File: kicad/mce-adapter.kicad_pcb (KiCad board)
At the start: 2 copper layers, 65.2 x 31.6 mm, 18 parts, among them J123 Conn_02x03_Odd_Even, J4 Conn_01x03_Male, U1 GAL16V8

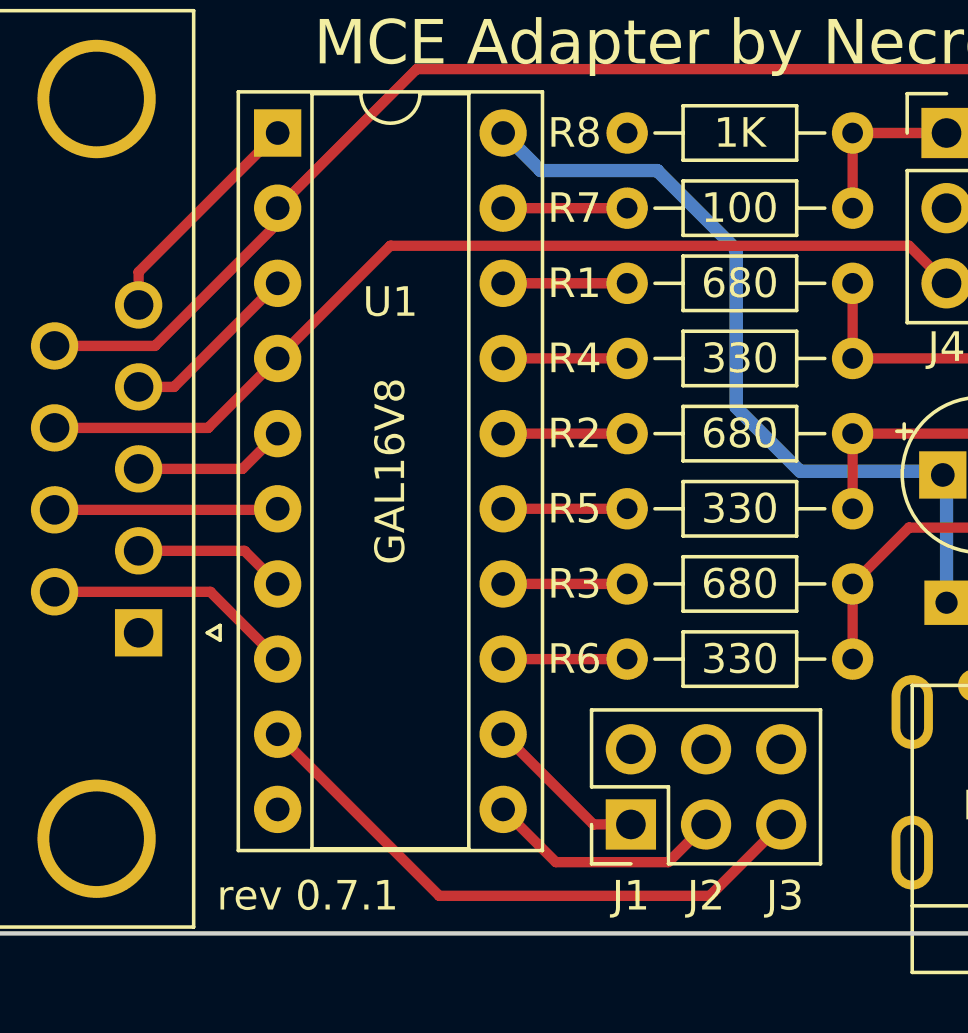
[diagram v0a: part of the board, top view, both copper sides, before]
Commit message: Readjusted resistor values, updated to version 0.7.2
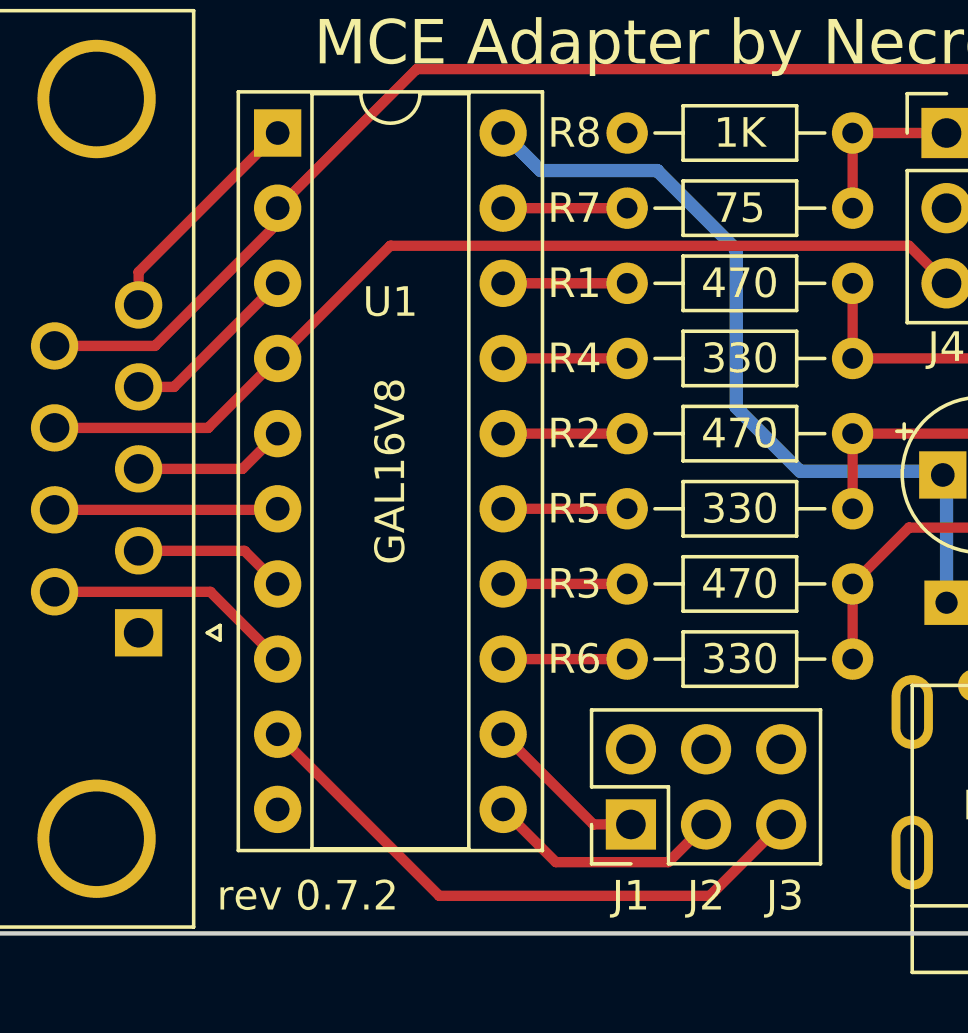
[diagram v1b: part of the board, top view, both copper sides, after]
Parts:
- R1, R2, R3: value 680 -> 470
- R7: value 100 -> 75
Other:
- board text added: "rev 0.7.2"
- board text removed: "rev 0.7.1"

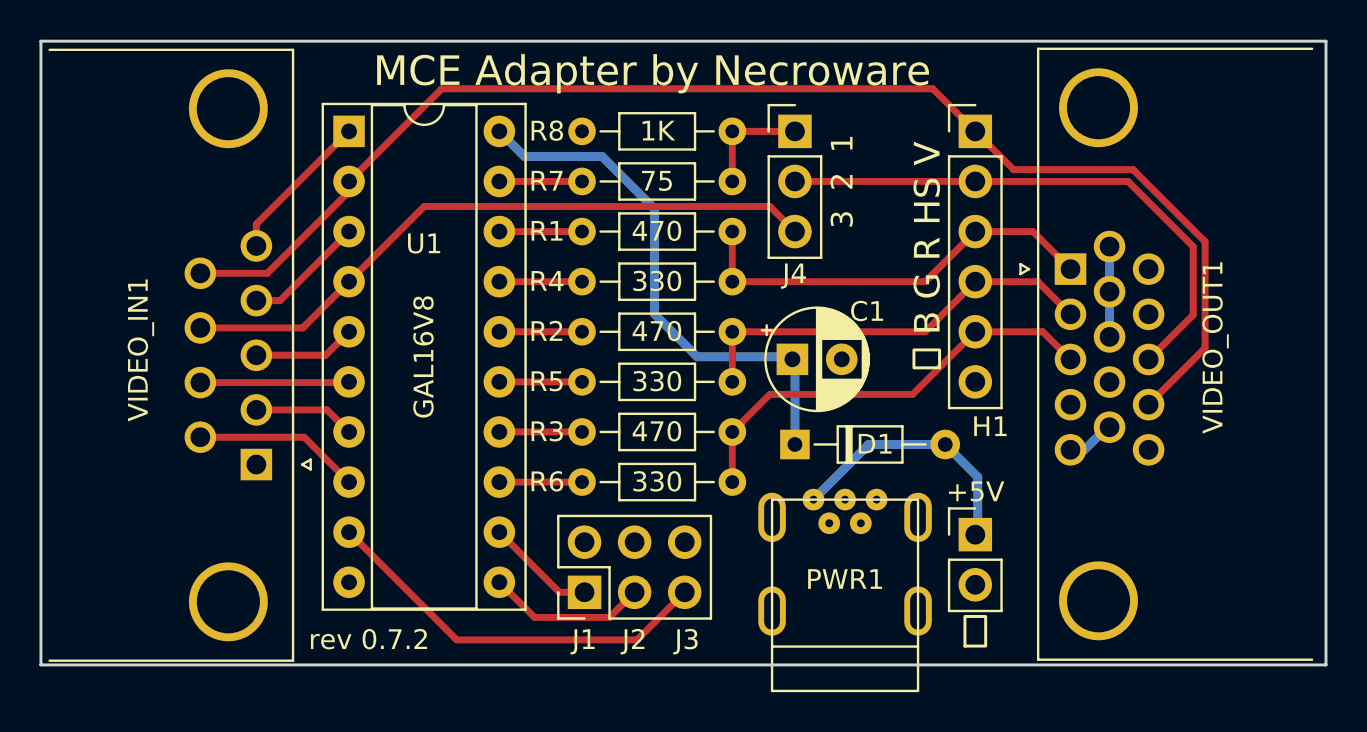
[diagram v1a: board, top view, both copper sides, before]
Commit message: Re-added DIP switch, rev. 0.8.0
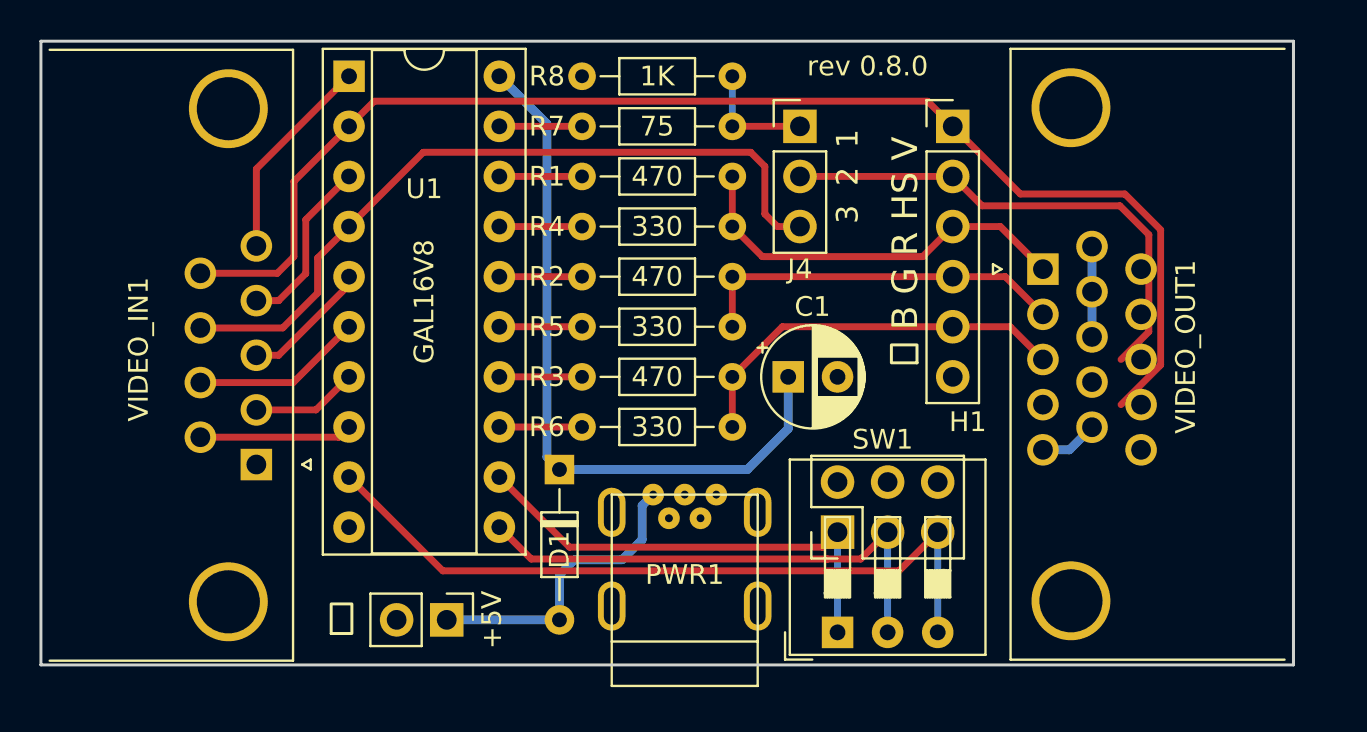
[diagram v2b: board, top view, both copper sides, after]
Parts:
- added REF**: OSHW-Symbol_6.7x6mm_SilkScreen, Symbol:OSHW-Symbol_6.7x6mm_SilkScreen, F.Cu at (169.8, 113.8)
- added SW1: SW_DIP_x03, Button_Switch_THT:SW_DIP_SPSTx03_Slide_9.78x9.8mm_W7.62mm_P2.54mm, F.Cu at (151.1, 116.7)
- moved PWR2 27.1 mm to (131.3, 116.1), turned to 270 degrees
- moved J123 13.2 mm to (151.1, 111.6)
- moved D1 12.0 mm to (137.0, 108.5), turned to 270 degrees
- moved PWR1 8.13 mm to (143.4, 109.7)
- moved R4 2.79 mm to (145.8, 96.1)
- moved R5 2.79 mm to (145.8, 101.2)
- moved R1 2.79 mm to (145.8, 93.6)
- moved R2 2.79 mm to (145.8, 98.7)
- moved R3 2.79 mm to (145.8, 103.8)
- moved R6 2.79 mm to (145.8, 106.3)
- moved R7 2.79 mm to (145.8, 91.1)
- moved R8 2.79 mm to (145.8, 88.5)
- moved U1 2.79 mm to (126.4, 88.5)
- moved VIDEO_OUT1 1.40 mm to (161.5, 98.3)
- moved H1 1.17 mm to (157.0, 91.1)
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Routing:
- net SW1_IN: track 5.58 -> 24.1 mm
- net SW2_IN: track 8.12 -> 26.0 mm
- net SW3_IN: track 20.3 -> 37.7 mm
- net Net-(C1-Pad1): track 27.1 -> 36.3 mm
- net H_IN: track 33.2 -> 38.1 mm
- net B_IN: track 7.76 -> 10.6 mm
- net G_IN: track 6.15 -> 8.90 mm
- net Net-(D1-Pad2): track 13.1 -> 15.6 mm
- net H_OUT: track 28.2 -> 25.8 mm
- net G_OUT: track 21.4 -> 19.1 mm
- net B_OUT: track 22.4 -> 20.0 mm
- net R_IN: track 5.19 -> 6.59 mm
- net IB_IN: track 7.55 -> 8.76 mm
- net R_OUT: track 21.5 -> 20.4 mm
- net IG_IN: track 8.48 -> 7.75 mm
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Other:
- board size 65.2 x 31.6 mm -> 63.5 x 31.6 mm
- board text added: "J1: color/mono J2: mode select J3: invert sync"
- board text added: "J4: sync S:1-2 H:2-3"
- board text added: "MCE Adapter"
- board text added: "by Necroware"
- board text added: "rev 0.8.0"
- board text removed: "J1: color/mono J2: mode select"
- board text removed: "J3: invert sync J4: sync S:1-2 H:2-3"
- board text removed: "MCE Adapter by Necroware"
- board text removed: "rev 0.7.2"

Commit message: Fixed GAL name
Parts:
- R7: value 75 -> 100
- U1: value GAL16V8 -> GAL16V8B
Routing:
- net GND: track 7.59 -> 0.15 mm
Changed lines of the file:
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@@
     (thickness 1.6)
     (drawings 9)
-    (tracks 104)
+    (tracks 101)
     (zones 0)
     (modules 20)
@@
     (fp_text value SW_DIP_x03 (at 3.81 8.5 270) (layer F.Fab) hide
       (effects (font (size 1 1) (thickness 0.15)))
-    )
-    (fp_text user on (at 0 -1.778 90) (layer F.Fab)
-      (effects (font (size 0.8 0.8) (thickness 0.12)))
-    )
-    (fp_text user %R (at 7.27 2.54) (layer F.Fab)
-      (effects (font (size 0.8 0.8) (thickness 0.12)))
     )
     (fp_line (start -0.08 -2.36) (end 8.7 -2.36) (layer F.Fab) (width 0.1))
@@
     (fp_line (start 8.95 7.75) (end 8.95 -2.7) (layer F.CrtYd) (width 0.05))
     (fp_line (start 8.95 -2.7) (end -1.35 -2.7) (layer F.CrtYd) (width 0.05))
+    (fp_text user on (at 0 -1.778 90) (layer F.Fab)
+      (effects (font (size 0.8 0.8) (thickness 0.12)))
+    )
+    (fp_text user %R (at 7.27 2.54) (layer F.Fab)
+      (effects (font (size 0.8 0.8) (thickness 0.12)))
+    )
     (pad 6 thru_hole oval (at 7.62 0 90) (size 1.6 1.6) (drill 0.8) (layers *.Cu *.Mask)
       (net 1 GND))
@@
       (effects (font (size 1 1) (thickness 0.15)))
     )
-    (fp_text value 75 (at 3.815 0) (layer F.SilkS)
+    (fp_text value 100 (at 3.815 0) (layer F.SilkS)
       (effects (font (size 1 1) (thickness 0.15)))
     )
@@
       (effects (font (size 1 1) (thickness 0.15)))
     )
-    (fp_text value GAL16V8 (at 3.81 11.43 90) (layer F.SilkS)
+    (fp_text value GAL16V8B (at 3.81 11.43 90) (layer F.SilkS)
       (effects (font (size 1 1) (thickness 0.15)))
     )
@@
   )
   (segment (start 164.032 101.681) (end 164.084 101.733) (width 0.45) (layer B.Cu) (net 1))
-  (segment (start 164.032 97.205) (end 164.032 101.681) (width 0.45) (layer B.Cu) (net 1))
   (segment (start 164.084 97.153) (end 164.032 97.205) (width 0.45) (layer B.Cu) (net 1))
-  (segment (start 162.887 107.458) (end 164.032 106.313) (width 0.45) (layer B.Cu) (net 1))
-  (segment (start 161.544 107.458) (end 162.887 107.458) (width 0.45) (layer B.Cu) (net 1))
   (segment (start 126.365 99.09637) (end 126.365 98.679) (width 0.35) (layer F.Cu) (net 2))
   (segment (start 122.79737 102.664) (end 126.365 99.09637) (width 0.35) (layer F.Cu) (net 2))
@@
   (segment (start 127.640001 89.783999) (end 155.696999 89.783999) (width 0.35) (layer F.Cu) (net 9))
   (segment (start 126.365 91.059) (end 127.640001 89.783999) (width 0.35) (layer F.Cu) (net 9))
+  (segment (start 168.621011 103.066989) (end 166.52 105.168) (width 0.35) (layer F.Cu) (net 9))
+  (segment (start 165.694543 94.488) (end 168.621011 97.414468) (width 0.35) (layer F.Cu) (net 9))
+  (segment (start 168.621011 97.414468) (end 168.621011 103.066989) (width 0.35) (layer F.Cu) (net 9))
   (segment (start 160.401 94.488) (end 165.694543 94.488) (width 0.35) (layer F.Cu) (net 9))
-  (segment (start 167.513 96.306457) (end 167.513 103.159) (width 0.35) (layer F.Cu) (net 9))
   (segment (start 156.972 91.059) (end 160.401 94.488) (width 0.35) (layer F.Cu) (net 9))
-  (segment (start 165.694543 94.488) (end 167.513 96.306457) (width 0.35) (layer F.Cu) (net 9))
-  (segment (start 167.513 103.159) (end 165.504 105.168) (width 0.35) (layer F.Cu) (net 9))
   (segment (start 131.826 116.078) (end 131.318 115.57) (width 0.45) (layer B.Cu) (net 10))
   (segment (start 136.906 116.078) (end 131.826 116.078) (width 0.45) (layer B.Cu) (net 10))
@@
   (segment (start 141.783 109.728) (end 141.224 110.287) (width 0.45) (layer B.Cu) (net 10))
   (segment (start 149.225 93.599) (end 156.972 93.599) (width 0.35) (layer F.Cu) (net 11))
+  (segment (start 168.021 97.663) (end 168.021 101.377) (width 0.35) (layer F.Cu) (net 11))
+  (segment (start 168.021 101.377) (end 166.52 102.878) (width 0.35) (layer F.Cu) (net 11))
+  (segment (start 165.446011 95.088011) (end 168.021 97.663) (width 0.35) (layer F.Cu) (net 11))
+  (segment (start 158.461011 95.088011) (end 165.446011 95.088011) (width 0.35) (layer F.Cu) (net 11))
   (segment (start 156.972 93.599) (end 158.461011 95.088011) (width 0.35) (layer F.Cu) (net 11))
-  (segment (start 158.461011 95.088011) (end 165.446011 95.088011) (width 0.35) (layer F.Cu) (net 11))
-  (segment (start 166.912989 96.554989) (end 166.912989 101.469011) (width 0.35) (layer F.Cu) (net 11))
-  (segment (start 166.912989 101.469011) (end 165.504 102.878) (width 0.35) (layer F.Cu) (net 11))
-  (segment (start 165.446011 95.088011) (end 166.912989 96.554989) (width 0.35) (layer F.Cu) (net 11))
   (segment (start 145.796 103.759) (end 145.796 106.299) (width 0.35) (layer F.Cu) (net 12) (status 30))
   (segment (start 145.796 103.759) (end 148.336 101.219) (width 0.35) (layer F.Cu) (net 12))
@@
   (segment (start 126.365 108.839) (end 131.121022 113.595022) (width 0.35) (layer F.Cu) (net 20))
   (segment (start 153.67 116.713) (end 153.67 111.633) (width 0.35) (layer B.Cu) (net 21))
-  (segment (start 151.13 116.713) (end 151.13 111.633) (width 0.35) (layer B.Cu) (net 22))
-  (segment (start 151.083916 116.713) (end 151.13 116.713) (width 0.35) (layer F.Cu) (net 22))
   (segment (start 150.616535 112.995011) (end 152.307989 112.995011) (width 0.35) (layer F.Cu) (net 21))
   (segment (start 150.616533 112.995009) (end 150.616535 112.995011) (width 0.35) (layer F.Cu) (net 21))
@@
   (segment (start 152.307989 112.995011) (end 153.67 111.633) (width 0.35) (layer F.Cu) (net 21))
   (segment (start 133.985 111.379) (end 135.601011 112.995011) (width 0.35) (layer F.Cu) (net 21))
+  (segment (start 151.13 116.713) (end 151.13 111.633) (width 0.35) (layer B.Cu) (net 22))
+  (segment (start 151.083916 116.713) (end 151.13 116.713) (width 0.35) (layer F.Cu) (net 22))
   (segment (start 150.368 112.395) (end 151.13 111.633) (width 0.35) (layer F.Cu) (net 22))
   (segment (start 137.541 112.395) (end 150.368 112.395) (width 0.35) (layer F.Cu) (net 22))

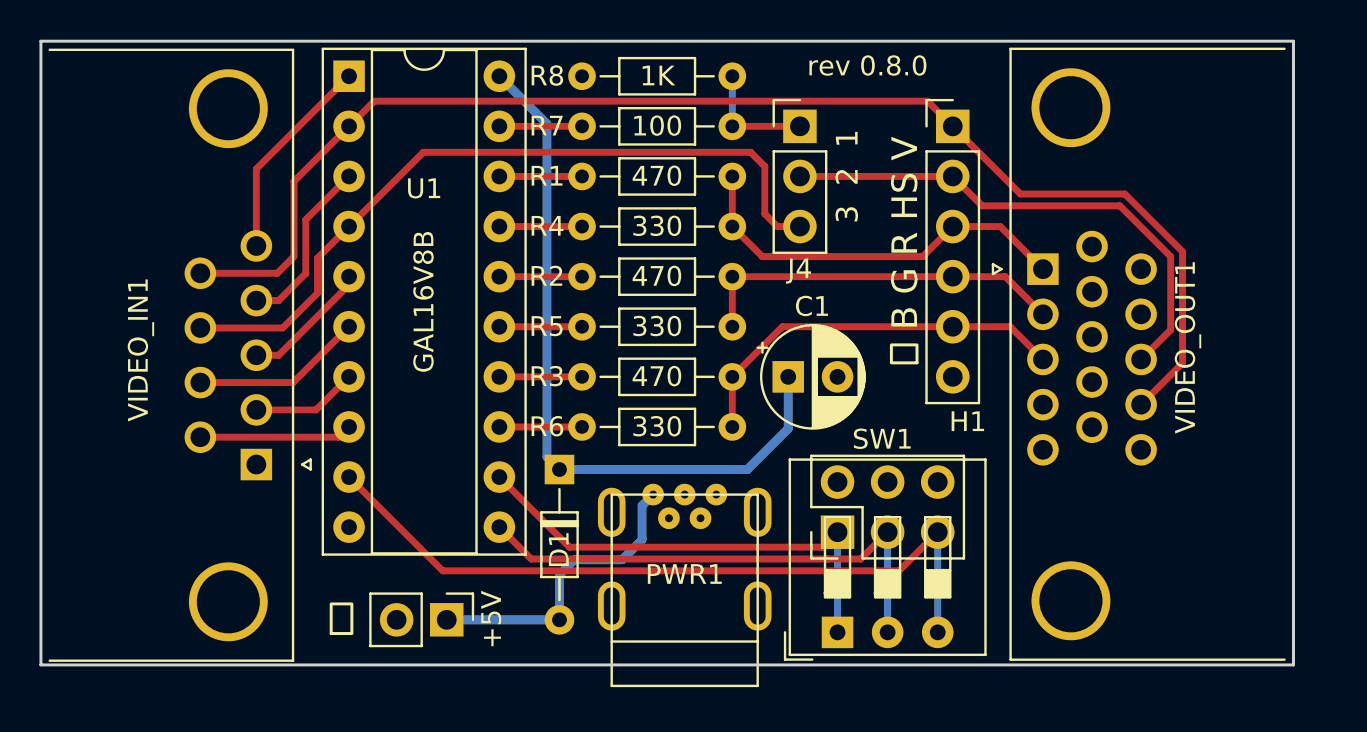
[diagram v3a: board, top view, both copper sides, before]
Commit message: Switched to KiCad 7
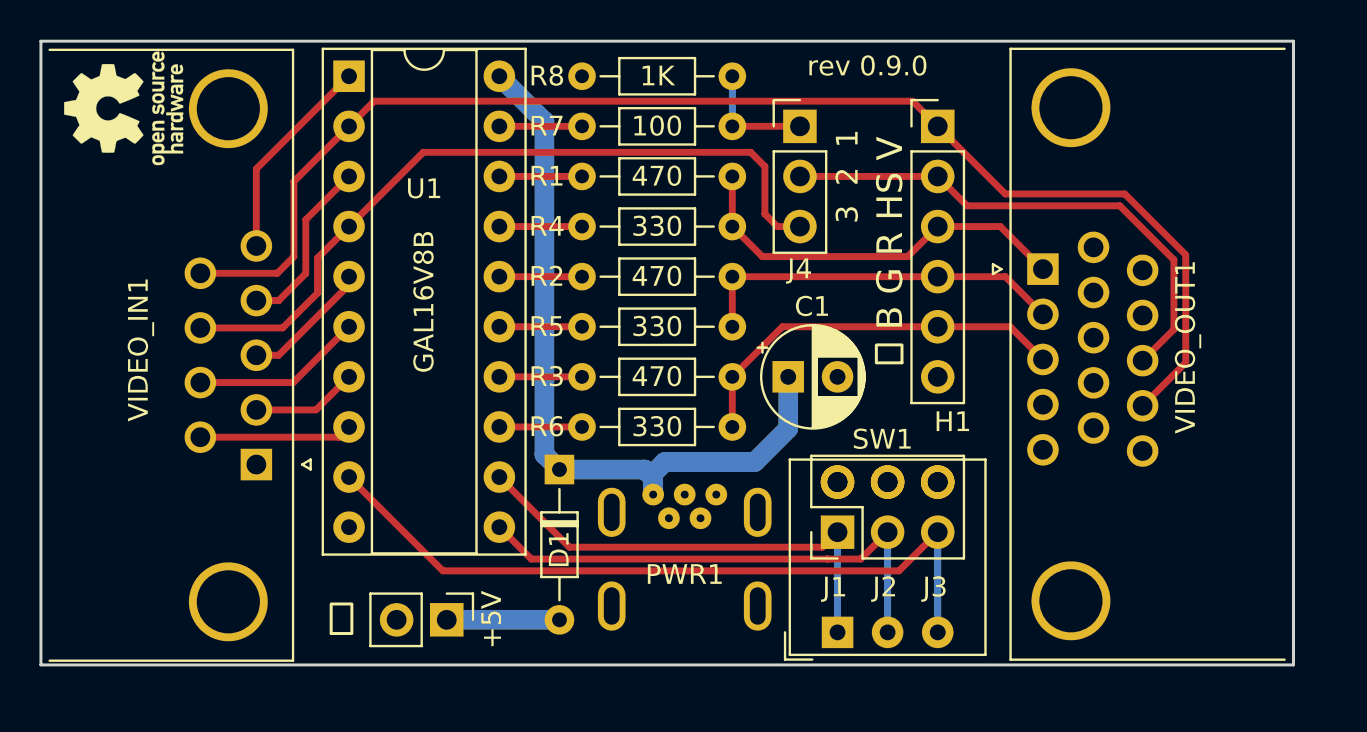
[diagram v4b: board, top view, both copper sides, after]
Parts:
- removed the REF** at (169.8, 113.8)
- added REF**: OSHW-Logo_5.7x6mm_SilkScreen, Symbol:OSHW-Logo_5.7x6mm_SilkScreen, F.Cu at (114.9, 90.2)
- moved H1 0.76 mm to (156.2, 91.1)
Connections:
- C1 pad 1: Net-(C1-Pad1) -> /VCC
- D1 pad 1: Net-(C1-Pad1) -> /VCC
- D1 pad 2: Net-(D1-Pad2) -> Net-(D1-A)
- PWR1 pad 1: Net-(D1-Pad2) -> /VCC
- PWR1 pad 2: (no net) -> unconnected-(PWR1-D--Pad2)
- PWR1 pad 3: (no net) -> unconnected-(PWR1-D+-Pad3)
- PWR1 pad 4: (no net) -> unconnected-(PWR1-ID-Pad4)
- PWR2 pad 1: Net-(D1-Pad2) -> Net-(D1-A)
- U1 pad 20: Net-(C1-Pad1) -> /VCC
- VIDEO_OUT1 pad 11: (no net) -> unconnected-(VIDEO_OUT1-Pad11)
- VIDEO_OUT1 pad 12: (no net) -> unconnected-(VIDEO_OUT1-Pad12)
- VIDEO_OUT1 pad 15: (no net) -> unconnected-(VIDEO_OUT1-Pad15)
- VIDEO_OUT1 pad 4: (no net) -> unconnected-(VIDEO_OUT1-Pad4)
- VIDEO_OUT1 pad 9: (no net) -> unconnected-(VIDEO_OUT1-Pad9)
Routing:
- net /VCC: track 0.00 -> 38.5 mm
- net Net-(C1-Pad1): track 36.3 -> 0.00 mm
- net Net-(D1-Pad2): track 15.6 -> 0.00 mm
- net Net-(D1-A): track 0.00 -> 5.71 mm
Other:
- net class Default removed
- net class Power removed
- board text added: "J3: color mode setting J4: sync S:1-2 H:2-3"
- board text added: "MDA - J1:on J2:on CGA/EGA - J1:off J2:n/a HiEGA - J1:on J2:off"
- board text added: "rev ${REVISION}"
- board text removed: "J1: color/mono J2: mode select J3: invert sync"
- board text removed: "J4: sync S:1-2 H:2-3"
- board text removed: "rev 0.8.0"
